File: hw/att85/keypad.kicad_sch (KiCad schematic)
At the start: 6 parts, among them SW401 SW_Push, SW402 SW_Push, SW403 SW_Push, SW404 SW_Push, SW405 SW_Push, SW406 SW_Push

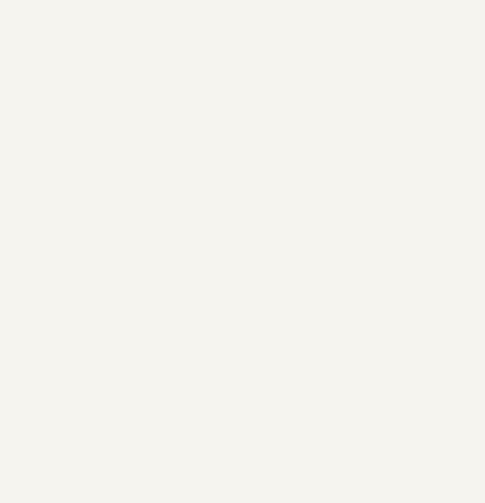
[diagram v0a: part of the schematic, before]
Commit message: chore(hw): wired basic connections, organized main sheet
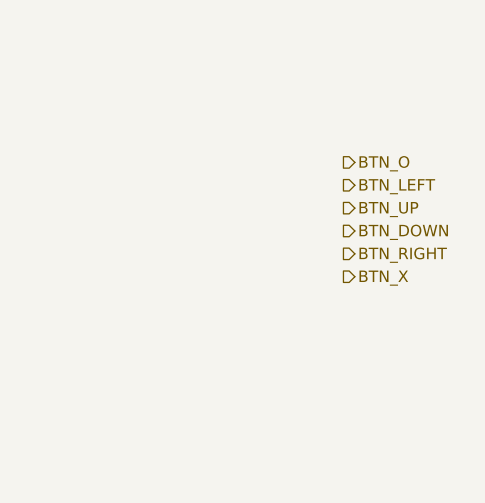
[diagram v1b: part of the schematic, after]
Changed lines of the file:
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@@
+		)
+	)
+	(hierarchical_label "BTN_UP"
+		(shape output)
+		(at 203.2 81.28 0)
+		(fields_autoplaced yes)
+		(effects
+			(font
+				(size 1.27 1.27)
+			)
+			(justify left)
+		)
+	)
+	(hierarchical_label "BTN_RIGHT"
+		(shape output)
+		(at 203.2 86.36 0)
+		(fields_autoplaced yes)
+		(effects
+			(font
+				(size 1.27 1.27)
+			)
+			(justify left)
+		)
+	)
+	(hierarchical_label "BTN_LEFT"
+		(shape output)
+		(at 203.2 78.74 0)
+		(fields_autoplaced yes)
+		(effects
+			(font
+				(size 1.27 1.27)
+			)
+			(justify left)
+		)
+	)
+	(hierarchical_label "BTN_DOWN"
+		(shape output)
+		(at 203.2 83.82 0)
+		(fields_autoplaced yes)
+		(effects
+			(font
+				(size 1.27 1.27)
+			)
+			(justify left)
+		)
+	)
+	(hierarchical_label "BTN_X"
+		(shape output)
+		(at 203.2 88.9 0)
+		(fields_autoplaced yes)
+		(effects
+			(font
+				(size 1.27 1.27)
+			)
+			(justify left)
+		)
+	)
+	(hierarchical_label "BTN_O"
+		(shape output)
+		(at 203.2 76.2 0)
+		(fields_autoplaced yes)
+		(effects
+			(font
+				(size 1.27 1.27)
+			)
+			(justify left)
 		)
 	)

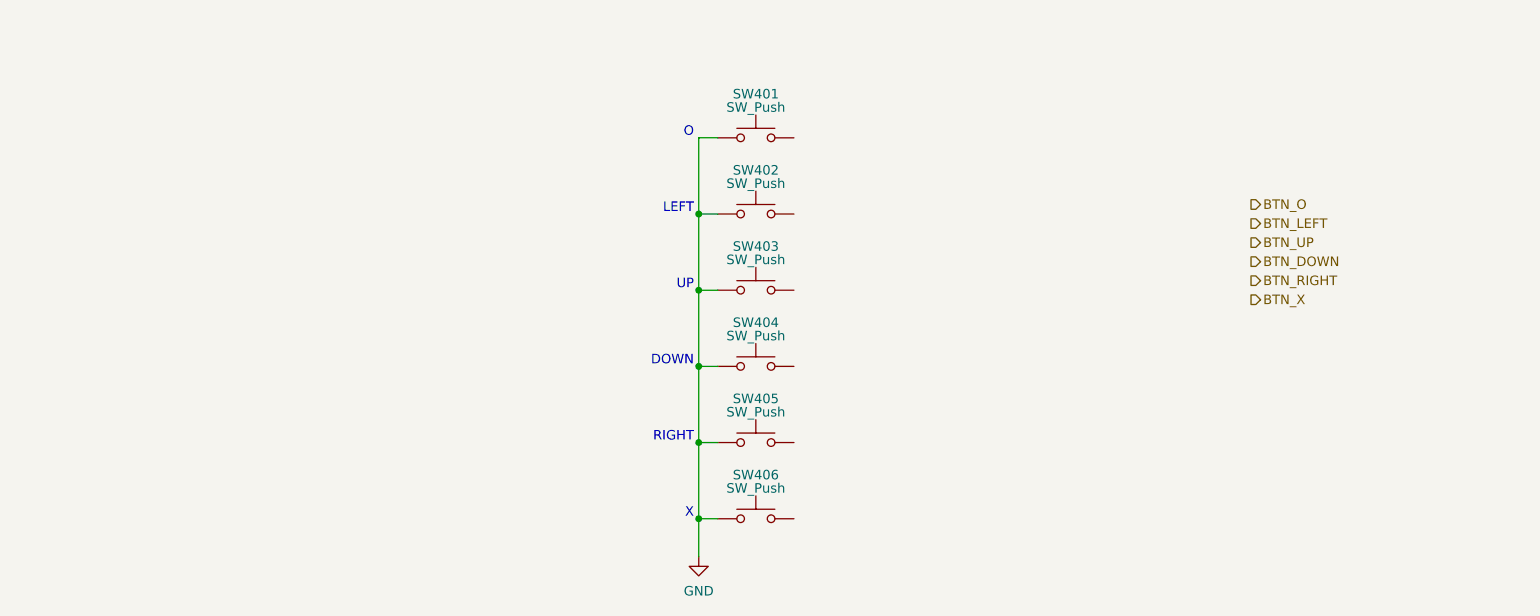
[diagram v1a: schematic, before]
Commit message: chore(hw): add keypad buffer
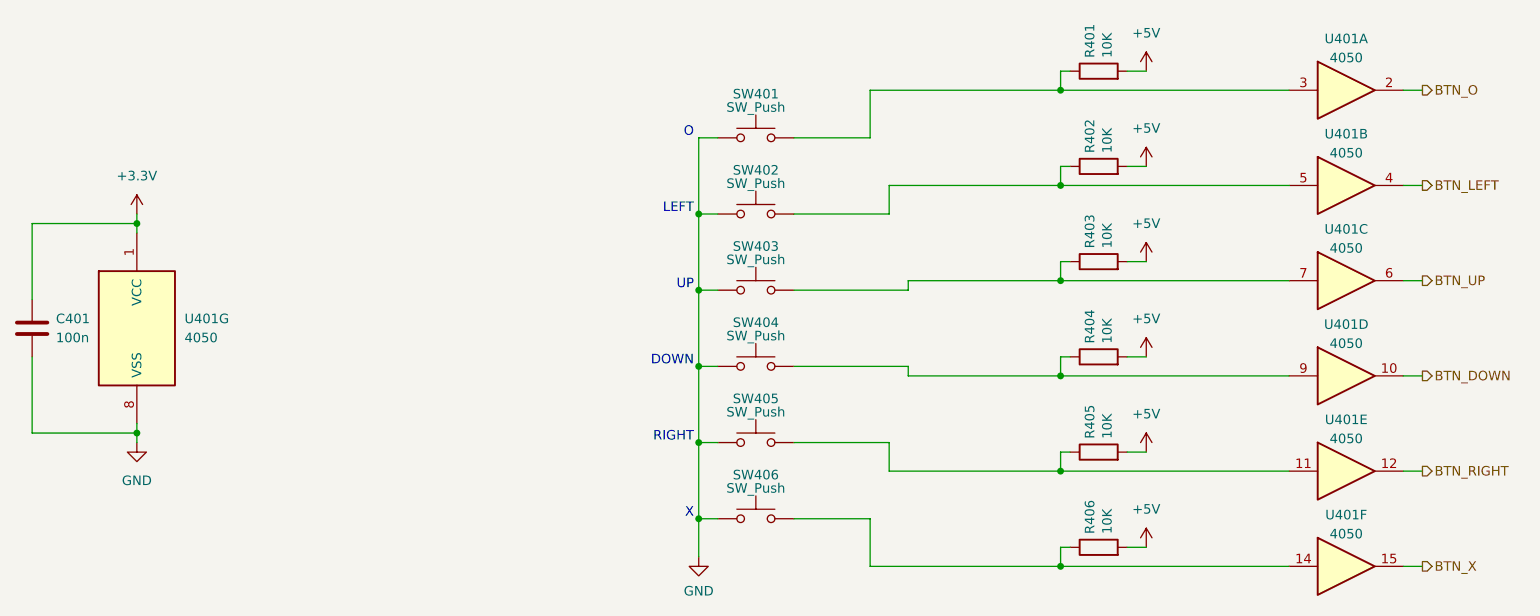
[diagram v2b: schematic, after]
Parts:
- added C401: 100n, Capacitor_SMD:C_0805_2012Metric_Pad1.18x1.45mm_HandSolder, symbol Device:C
- added R401, R402, R403, R404, R405, R406: 10K, Resistor_SMD:R_0805_2012Metric_Pad1.20x1.40mm_HandSolder, symbol Device:R
- added U401: 4050, Package_SO:SOIC-16_3.9x9.9mm_P1.27mm, symbol 4xxx:4050
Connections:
- net BTN_DOWN: now also U401.10
- net BTN_LEFT: now also U401.4
- net BTN_O: now also U401.2
- net BTN_RIGHT: now also U401.12
- net BTN_UP: now also U401.6
- net BTN_X: now also U401.15
- net GND: now also C401.2, U401.8 (VSS)
- net at SW405.2: now also R405.1, U401.11
- net at SW406.2: now also R406.1, U401.14
- net at SW403.2: now also R403.1, U401.7
- net at SW404.2: now also R404.1, U401.9
- net at SW401.2: now also R401.1, U401.3
- net at SW402.2: now also R402.1, U401.5
- new net +3.3V: C401.1, U401.1 (VCC)
- new net +5V: R401.2, R402.2, R403.2, R404.2, R405.2, R406.2

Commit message: chore(hw): prepare layout
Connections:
- net BTN_DOWN: now also U401.6; no longer U401.10
- net BTN_RIGHT: now also U401.15; no longer U401.12
- net BTN_UP: now also U401.10; no longer U401.6
- net BTN_X: now also U401.12; no longer U401.15
- net at R404.1, SW404.2: now also U401.7; no longer U401.9
- net at R406.1, SW406.2: now also U401.11; no longer U401.14
- net at R405.1, SW405.2: now also U401.14; no longer U401.11
- net at R403.1, SW403.2: now also U401.9; no longer U401.7
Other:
- moved on the sheet: U401C, U401D, U401E, U401F
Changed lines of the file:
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@@
 		)
 		(instances
-			(project ""
+			(project "att85"
 				(path "/fc4ba96f-a9f8-4f1a-a9c5-2b16679a6770/92669e5a-b445-42f6-941a-fe6cd3da5605"
 					(reference "#PWR0402")
@@
 	(symbol
 		(lib_id "4xxx:4050")
-		(at 215.9 99.06 0)
+		(at 215.9 86.36 0)
 		(unit 4)
 		(exclude_from_sim no)
@@
 		(dnp no)
 		(property "Reference" "U401"
-			(at 215.9 92.202 0)
+			(at 215.9 79.502 0)
 			(effects
 				(font
@@
 		)
 		(property "Value" "4050"
-			(at 215.9 94.742 0)
+			(at 215.9 82.042 0)
 			(effects
 				(font
@@
 		)
 		(property "Footprint" "Package_SO:SOIC-16_3.9x9.9mm_P1.27mm"
-			(at 215.9 99.06 0)
+			(at 215.9 86.36 0)
 			(effects
 				(font
@@
 		)
 		(property "Datasheet" "http://www.intersil.com/content/dam/intersil/documents/cd40/cd4050bms.pdf"
-			(at 215.9 99.06 0)
+			(at 215.9 86.36 0)
 			(effects
 				(font
@@
 		)
 		(property "Description" "Hex Buffer"
-			(at 215.9 99.06 0)
+			(at 215.9 86.36 0)
 			(effects
 				(font
@@
 		)
 		(instances
-			(project ""
+			(project "att85"
 				(path "/fc4ba96f-a9f8-4f1a-a9c5-2b16679a6770/92669e5a-b445-42f6-941a-fe6cd3da5605"
 					(reference "U401")
@@
 		)
 		(instances
-			(project ""
+			(project "att85"
 				(path "/fc4ba96f-a9f8-4f1a-a9c5-2b16679a6770/92669e5a-b445-42f6-941a-fe6cd3da5605"
 					(reference "U401")
@@
 		)
 		(instances
-			(project ""
+			(project "att85"
 				(path "/fc4ba96f-a9f8-4f1a-a9c5-2b16679a6770/92669e5a-b445-42f6-941a-fe6cd3da5605"
 					(reference "U401")
@@
 		)
 		(instances
-			(project ""
+			(project "att85"
 				(path "/fc4ba96f-a9f8-4f1a-a9c5-2b16679a6770/92669e5a-b445-42f6-941a-fe6cd3da5605"
 					(reference "U401")
@@
 	(symbol
 		(lib_id "4xxx:4050")
-		(at 215.9 86.36 0)
+		(at 215.9 99.06 0)
 		(unit 3)
 		(exclude_from_sim no)
@@
 		(dnp no)
 		(property "Reference" "U401"
-			(at 215.9 79.502 0)
+			(at 215.9 92.202 0)
 			(effects
 				(font
@@
 		)
 		(property "Value" "4050"
-			(at 215.9 82.042 0)
+			(at 215.9 94.742 0)
 			(effects
 				(font
@@
 		)
 		(property "Footprint" "Package_SO:SOIC-16_3.9x9.9mm_P1.27mm"
-			(at 215.9 86.36 0)
+			(at 215.9 99.06 0)
 			(effects
 				(font
@@
 		)
 		(property "Datasheet" "http://www.intersil.com/content/dam/intersil/documents/cd40/cd4050bms.pdf"
-			(at 215.9 86.36 0)
+			(at 215.9 99.06 0)
 			(effects
 				(font
@@
 		)
 		(property "Description" "Hex Buffer"
-			(at 215.9 86.36 0)
+			(at 215.9 99.06 0)
 			(effects
 				(font
@@
 		)
 		(instances
-			(project ""
+			(project "att85"
 				(path "/fc4ba96f-a9f8-4f1a-a9c5-2b16679a6770/92669e5a-b445-42f6-941a-fe6cd3da5605"
 					(reference "U401")
@@
 	(symbol
 		(lib_id "4xxx:4050")
-		(at 215.9 124.46 0)
+		(at 215.9 111.76 0)
 		(unit 6)
 		(exclude_from_sim no)
@@
 		(dnp no)
 		(property "Reference" "U401"
-			(at 215.9 117.602 0)
+			(at 215.9 104.902 0)
 			(effects
 				(font
@@
 		)
 		(property "Value" "4050"
-			(at 215.9 120.142 0)
+			(at 215.9 107.442 0)
 			(effects
 				(font
@@
 		)
 		(property "Footprint" "Package_SO:SOIC-16_3.9x9.9mm_P1.27mm"
-			(at 215.9 124.46 0)
+			(at 215.9 111.76 0)
 			(effects
 				(font
@@
 		)
 		(property "Datasheet" "http://www.intersil.com/content/dam/intersil/documents/cd40/cd4050bms.pdf"
-			(at 215.9 124.46 0)
+			(at 215.9 111.76 0)
 			(effects
 				(font
@@
 		)
 		(property "Description" "Hex Buffer"
-			(at 215.9 124.46 0)
+			(at 215.9 111.76 0)
 			(effects
 				(font
@@
 		)
 		(instances
-			(project ""
+			(project "att85"
 				(path "/fc4ba96f-a9f8-4f1a-a9c5-2b16679a6770/92669e5a-b445-42f6-941a-fe6cd3da5605"
 					(reference "U401")
@@
 		)
 		(instances
-			(project ""
+			(project "att85"
 				(path "/fc4ba96f-a9f8-4f1a-a9c5-2b16679a6770/92669e5a-b445-42f6-941a-fe6cd3da5605"
 					(reference "#PWR02")
@@
 	(symbol
 		(lib_id "4xxx:4050")
-		(at 215.9 111.76 0)
+		(at 215.9 124.46 0)
 		(unit 5)
 		(exclude_from_sim no)
@@
 		(dnp no)
 		(property "Reference" "U401"
-			(at 215.9 104.902 0)
+			(at 215.9 117.602 0)
 			(effects
 				(font
@@
 		)
 		(property "Value" "4050"
-			(at 215.9 107.442 0)
+			(at 215.9 120.142 0)
 			(effects
 				(font
@@
 		)
 		(property "Footprint" "Package_SO:SOIC-16_3.9x9.9mm_P1.27mm"
-			(at 215.9 111.76 0)
+			(at 215.9 124.46 0)
 			(effects
 				(font
@@
 		)
 		(property "Datasheet" "http://www.intersil.com/content/dam/intersil/documents/cd40/cd4050bms.pdf"
-			(at 215.9 111.76 0)
+			(at 215.9 124.46 0)
 			(effects
 				(font
@@
 		)
 		(property "Description" "Hex Buffer"
-			(at 215.9 111.76 0)
+			(at 215.9 124.46 0)
 			(effects
 				(font
@@
 		)
 		(instances
-			(project ""
+			(project "att85"
 				(path "/fc4ba96f-a9f8-4f1a-a9c5-2b16679a6770/92669e5a-b445-42f6-941a-fe6cd3da5605"
 					(reference "U401")
@@
 		)
 		(instances
-			(project ""
+			(project "att85"
 				(path "/fc4ba96f-a9f8-4f1a-a9c5-2b16679a6770/92669e5a-b445-42f6-941a-fe6cd3da5605"
 					(reference "#PWR0403")
@@
 		)
 		(instances
-			(project ""
+			(project "att85"
 				(path "/fc4ba96f-a9f8-4f1a-a9c5-2b16679a6770/92669e5a-b445-42f6-941a-fe6cd3da5605"
 					(reference "#PWR03")
